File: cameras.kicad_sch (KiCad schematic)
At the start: 2 parts, among them J1 F32Q-1A7H1-11022, J2 F32Q-1A7H1-11022

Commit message: annotations, small fixes
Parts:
- renumbered J2 to J1, J1 to J2
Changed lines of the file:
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@@
 		(on_board yes)
 		(dnp no)
-		(property "Reference" "#PWR0134"
+		(property "Reference" "#PWR05"
 			(at 115.57 132.08 0)
 			(effects
@@
 			(project "CUTIE-CITRUS"
 				(path "/40af415e-5e3a-41a5-ab07-08c2181863e4/15df30c6-bd70-4c9b-9319-89653597e067"
-					(reference "#PWR0134")
+					(reference "#PWR05")
 					(unit 1)
 				)
@@
 		(on_board yes)
 		(dnp no)
-		(property "Reference" "#PWR0103"
+		(property "Reference" "#PWR06"
 			(at 200.66 132.08 0)
 			(effects
@@
 			(project "CUTIE-CITRUS"
 				(path "/40af415e-5e3a-41a5-ab07-08c2181863e4/15df30c6-bd70-4c9b-9319-89653597e067"
-					(reference "#PWR0103")
+					(reference "#PWR06")
 					(unit 1)
 				)
@@
 		(on_board yes)
 		(dnp no)
-		(property "Reference" "J2"
+		(property "Reference" "J1"
 			(at 128.27 63.5 0)
 			(effects
@@
 			(project "CUTIE-CITRUS"
 				(path "/40af415e-5e3a-41a5-ab07-08c2181863e4/15df30c6-bd70-4c9b-9319-89653597e067"
-					(reference "J2")
+					(reference "J1")
 					(unit 1)
 				)
@@
 		(on_board yes)
 		(dnp no)
-		(property "Reference" "J1"
+		(property "Reference" "J2"
 			(at 213.36 63.5 0)
 			(effects
@@
 			(project "CUTIE-CITRUS"
 				(path "/40af415e-5e3a-41a5-ab07-08c2181863e4/15df30c6-bd70-4c9b-9319-89653597e067"
-					(reference "J1")
+					(reference "J2")
 					(unit 1)
 				)

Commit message: extra abstraction layer for cm5 conns.
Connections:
- net SCL0 renamed I2C0.SCL
- net SCL1 renamed I2C1.SCL
- net SDA0 renamed I2C0.SDA
- net SDA1 renamed I2C1.SDA
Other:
- company: (none) -> Andre S Winkel | Highlander Space Program | University of California, Riverside
- title: (none) -> CUTIE-CITRUS PCB
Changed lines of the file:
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@@
 	(generator_version "9.0")
 	(paper "A4")
+	(title_block
+		(title "CUTIE-CITRUS PCB")
+		(date "2025-11-24")
+		(rev "A")
+		(company "Andre S Winkel | Highlander Space Program | University of California, Riverside")
+	)
 	(bus_alias "DPHY"
 		(members "D0_N" "D0_P" "D1_N" "D1_P" "C_N" "C_P" "D2_N" "D2_P" "D3_N" "D3_P")
@@
 	)
 	(bus_entry
+		(at 165.1 119.38)
+		(size 2.54 2.54)
+		(stroke
+			(width 0)
+			(type default)
+		)
+	)
+	(bus_entry
 		(at 165.1 88.9)
 		(size 2.54 2.54)
@@
 	)
 	(bus_entry
+		(at 165.1 116.84)
+		(size 2.54 2.54)
+		(stroke
+			(width 0)
+			(type default)
+		)
+	)
+	(bus_entry
 		(at 165.1 78.74)
 		(size 2.54 2.54)
@@
 	)
 	(bus_entry
+		(at 80.01 119.38)
+		(size 2.54 2.54)
+		(stroke
+			(width 0)
+			(type default)
+		)
+	)
+	(bus_entry
 		(at 165.1 93.98)
 		(size 2.54 2.54)
@@
 	)
 	(bus_entry
+		(at 80.01 116.84)
+		(size 2.54 2.54)
+		(stroke
+			(width 0)
+			(type default)
+		)
+	)
+	(bus_entry
 		(at 80.01 88.9)
 		(size 2.54 2.54)
@@
 		)
 	)
+	(bus
+		(pts
+			(xy 165.1 119.38) (xy 165.1 116.84)
+		)
+		(stroke
+			(width 0)
+			(type default)
+		)
+	)
 	(wire
 		(pts
@@
 		)
 	)
+	(bus
+		(pts
+			(xy 80.01 119.38) (xy 80.01 116.84)
+		)
+		(stroke
+			(width 0)
+			(type default)
+		)
+	)
+	(wire
+		(pts
+			(xy 82.55 119.38) (xy 118.11 119.38)
+		)
+		(stroke
+			(width 0)
+			(type default)
+		)
+	)
 	(wire
 		(pts
@@
 		)
 	)
-	(wire
-		(pts
-			(xy 161.29 121.92) (xy 203.2 121.92)
-		)
-		(stroke
-			(width 0)
-			(type solid)
-		)
-	)
 	(bus
 		(pts
@@
 	(wire
 		(pts
-			(xy 76.2 111.76) (xy 118.11 111.76)
+			(xy 99.06 111.76) (xy 118.11 111.76)
 		)
 		(stroke
@@
 	(wire
 		(pts
+			(xy 167.64 121.92) (xy 203.2 121.92)
+		)
+		(stroke
+			(width 0)
+			(type default)
+		)
+	)
+	(wire
+		(pts
 			(xy 200.66 78.74) (xy 203.2 78.74)
 		)
@@
 		)
 	)
-	(wire
-		(pts
-			(xy 76.2 114.3) (xy 118.11 114.3)
+	(bus
+		(pts
+			(xy 165.1 116.84) (xy 165.1 110.49)
+		)
+		(stroke
+			(width 0)
+			(type default)
+		)
+	)
+	(wire
+		(pts
+			(xy 99.06 114.3) (xy 118.11 114.3)
 		)
 		(stroke
@@
 	(bus
 		(pts
+			(xy 161.29 110.49) (xy 165.1 110.49)
+		)
+		(stroke
+			(width 0)
+			(type default)
+		)
+	)
+	(bus
+		(pts
 			(xy 80.01 78.74) (xy 80.01 81.28)
 		)
@@
 	(bus
 		(pts
+			(xy 80.01 116.84) (xy 80.01 110.49)
+		)
+		(stroke
+			(width 0)
+			(type default)
+		)
+	)
+	(wire
+		(pts
+			(xy 82.55 121.92) (xy 118.11 121.92)
+		)
+		(stroke
+			(width 0)
+			(type default)
+		)
+	)
+	(bus
+		(pts
 			(xy 80.01 88.9) (xy 80.01 93.98)
 		)
@@
 	(wire
 		(pts
-			(xy 76.2 121.92) (xy 118.11 121.92)
-		)
-		(stroke
-			(width 0)
-			(type solid)
-		)
-	)
-	(wire
-		(pts
 			(xy 167.64 104.14) (xy 203.2 104.14)
 		)
@@
 	(wire
 		(pts
-			(xy 76.2 119.38) (xy 118.11 119.38)
-		)
-		(stroke
-			(width 0)
-			(type solid)
-		)
-	)
-	(wire
-		(pts
 			(xy 167.64 73.66) (xy 203.2 73.66)
 		)
@@
 		)
 	)
+	(wire
+		(pts
+			(xy 167.64 119.38) (xy 203.2 119.38)
+		)
+		(stroke
+			(width 0)
+			(type default)
+		)
+	)
 	(bus
 		(pts
@@
 	(wire
 		(pts
-			(xy 161.29 119.38) (xy 203.2 119.38)
-		)
-		(stroke
-			(width 0)
-			(type solid)
-		)
-	)
-	(wire
-		(pts
 			(xy 82.55 73.66) (xy 118.11 73.66)
 		)
@@
 			(width 0)
 			(type solid)
+		)
+	)
+	(bus
+		(pts
+			(xy 76.2 110.49) (xy 80.01 110.49)
+		)
+		(stroke
+			(width 0)
+			(type default)
 		)
 	)
@@
 		)
 	)
-	(label "SDA1"
+	(label "I2C1.SDA"
 		(at 195.58 121.92 180)
 		(effects
@@
 		)
 	)
-	(label "SCL0"
+	(label "I2C0.SCL"
 		(at 110.49 119.38 180)
 		(effects
@@
 		)
 	)
-	(label "SCL1"
+	(label "I2C1.SCL"
 		(at 195.58 119.38 180)
 		(effects
@@
 		)
 	)
-	(label "SDA0"
+	(label "I2C0.SDA"
 		(at 110.49 121.92 180)
 		(effects
@@
 	(hierarchical_label "CAM_GPIO0"
 		(shape input)
-		(at 76.2 111.76 180)
+		(at 99.06 111.76 180)
 		(effects
 			(font
@@
 		)
 	)
-	(hierarchical_label "SCL0"
-		(shape input)
-		(at 76.2 119.38 180)
-		(effects
-			(font
-				(size 1.27 1.27)
-			)
-			(justify right)
-		)
-	)
-	(hierarchical_label "SDA1"
-		(shape input)
-		(at 161.29 121.92 180)
-		(effects
-			(font
-				(size 1.27 1.27)
-			)
-			(justify right)
-		)
-	)
 	(hierarchical_label "DPHY1{DPHY}"
 		(shape bidirectional)
@@
 		)
 	)
-	(hierarchical_label "SCL1"
-		(shape input)
-		(at 161.29 119.38 180)
+	(hierarchical_label "I2C0{I2C}"
+		(shape bidirectional)
+		(at 76.2 110.49 180)
 		(effects
 			(font
@@
 		)
 	)
-	(hierarchical_label "SDA0"
-		(shape input)
-		(at 76.2 121.92 180)
+	(hierarchical_label "I2C1{I2C}"
+		(shape bidirectional)
+		(at 161.29 110.49 180)
 		(effects
 			(font
@@
 	(hierarchical_label "CAM_GPIO1"
 		(shape input)
-		(at 76.2 114.3 180)
-		(effects
-			(font
+		(at 99.06 114.3 180)
+		(effects
+			(font

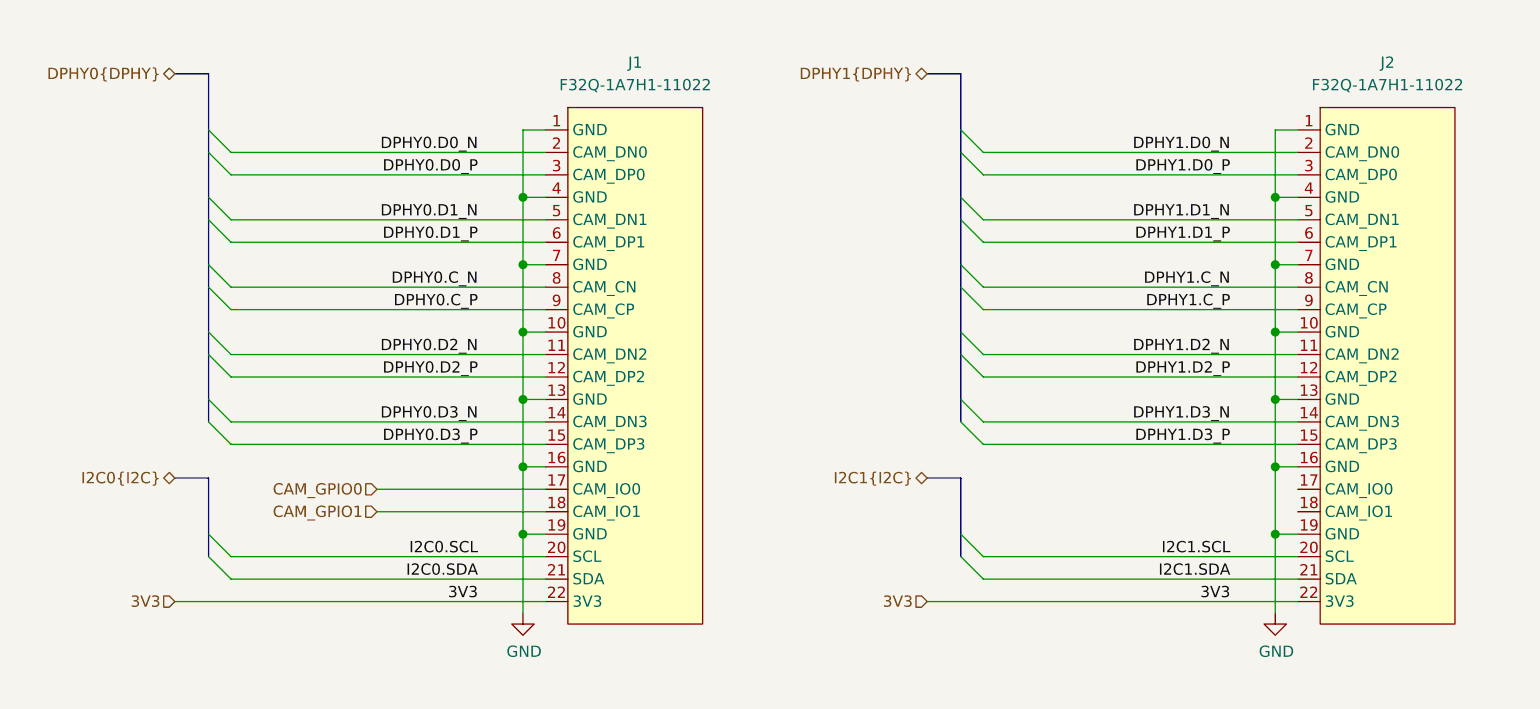
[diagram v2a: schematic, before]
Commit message: prepared usb3, abstracted cameras, backplane connector
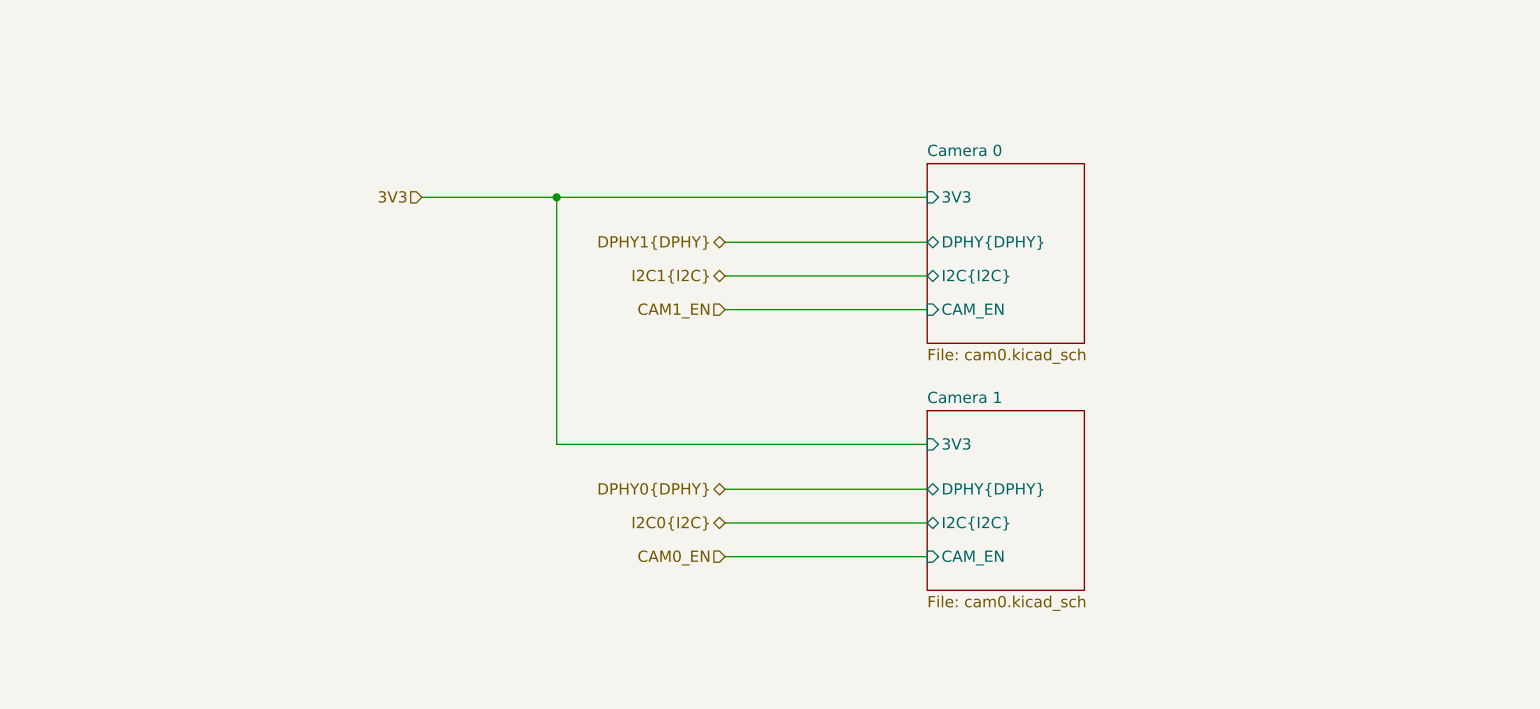
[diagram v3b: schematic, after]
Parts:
- removed J1, J2: F32Q-1A7H1-11022, library:Hirose_FH12-22S-0.5SH_1x22-1MP_P0.50mm_Horizontal, symbol library:F32Q-1A7H1-11022
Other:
- added sheet Camera 0 (cam0.kicad_sch)
- added sheet Camera 1 (cam0.kicad_sch)

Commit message: un-abstraction, footprints, layout edge cuts
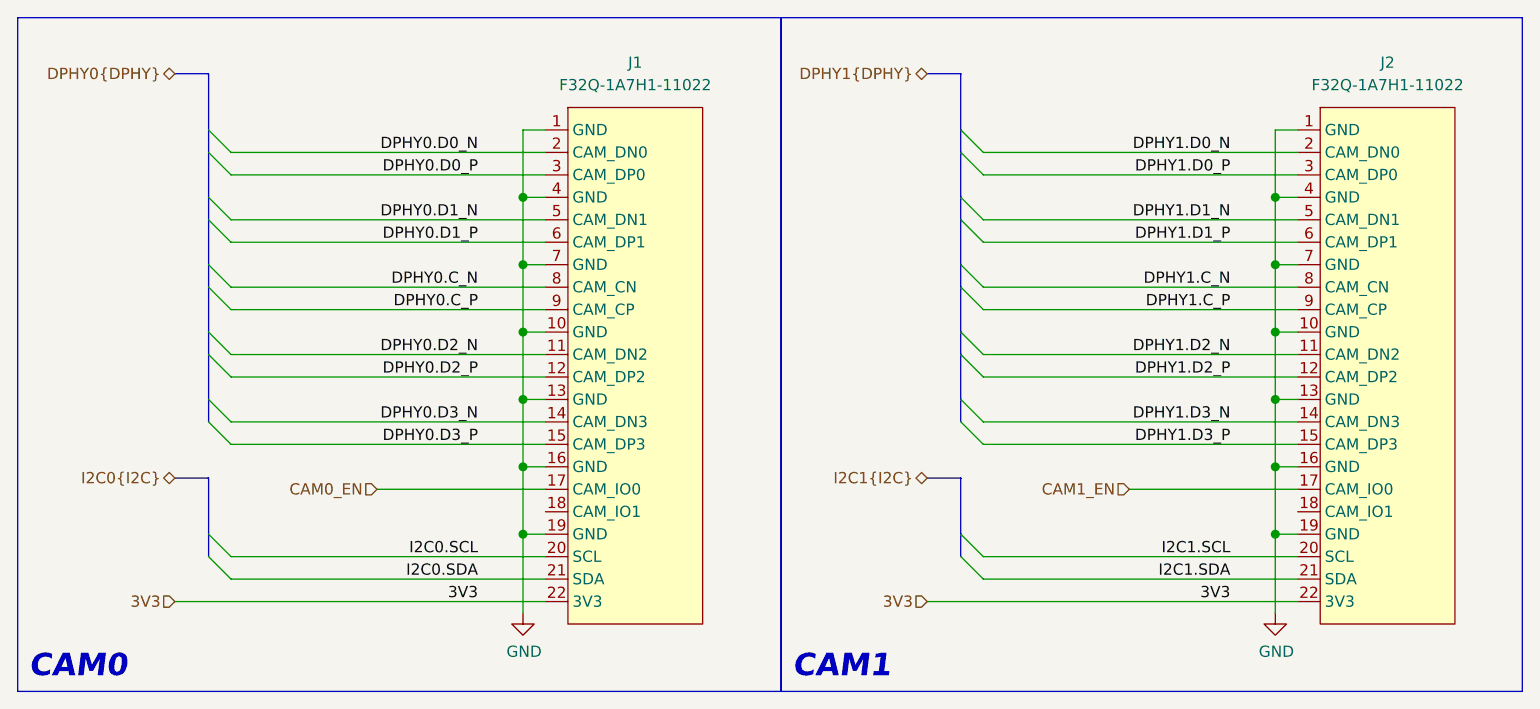
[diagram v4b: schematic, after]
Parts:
- added J1, J2: F32Q-1A7H1-11022, library:Hirose_FH12-22S-0.5SH_1x22-1MP_P0.50mm_Horizontal, symbol library:F32Q-1A7H1-11022
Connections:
- net 3V3: now also J1.22 (3V3), J2.22 (3V3)
- net CAM0_EN: now also J1.17 (CAM_IO0)
- net CAM1_EN: now also J2.17 (CAM_IO0)
- new net DPHY0.C_N: J1.8 (CAM_CN)
- new net DPHY0.C_P: J1.9 (CAM_CP)
- new net DPHY0.D0_N: J1.2 (CAM_DN0)
- new net DPHY0.D0_P: J1.3 (CAM_DP0)
- new net DPHY0.D1_N: J1.5 (CAM_DN1)
- new net DPHY0.D1_P: J1.6 (CAM_DP1)
- new net DPHY0.D2_N: J1.11 (CAM_DN2)
- new net DPHY0.D2_P: J1.12 (CAM_DP2)
- new net DPHY0.D3_N: J1.14 (CAM_DN3)
- new net DPHY0.D3_P: J1.15 (CAM_DP3)
- new net DPHY1.C_N: J2.8 (CAM_CN)
- new net DPHY1.C_P: J2.9 (CAM_CP)
- new net DPHY1.D0_N: J2.2 (CAM_DN0)
- new net DPHY1.D0_P: J2.3 (CAM_DP0)
- new net DPHY1.D1_N: J2.5 (CAM_DN1)
- new net DPHY1.D1_P: J2.6 (CAM_DP1)
- new net DPHY1.D2_N: J2.11 (CAM_DN2)
- new net DPHY1.D2_P: J2.12 (CAM_DP2)
- new net DPHY1.D3_N: J2.14 (CAM_DN3)
- new net DPHY1.D3_P: J2.15 (CAM_DP3)
- new net GND: J1.1 (GND), J1.10 (GND), J1.13 (GND), J1.16 (GND), J1.19 (GND), J1.4 (GND), J1.7 (GND), J2.1 (GND), J2.10 (GND), J2.13 (GND), J2.16 (GND), J2.19 (GND), J2.4 (GND), J2.7 (GND)
- new net I2C0.SCL: J1.20 (SCL)
- new net I2C0.SDA: J1.21 (SDA)
- new net I2C1.SCL: J2.20 (SCL)
- new net I2C1.SDA: J2.21 (SDA)
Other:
- removed sheet Camera 0
- removed sheet Camera 1
- note added: "CAM0"
- note added: "CAM1"

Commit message: redid gpio layout, removed one temp sensor, bom
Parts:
- J1, J2: Manufacturer (none) -> Amphenol ICC (FCI); Manufacturer Product Number (none) -> F32Q-1A7H1-11022
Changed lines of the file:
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@@
+			)
+		)
+		(property "Manufacturer" "Amphenol ICC (FCI)"
+			(at 128.27 97.79 0)
+			(effects
+				(font
+					(size 1.27 1.27)
+				)
+				(hide yes)
+			)
+		)
+		(property "Manufacturer Product Number" "F32Q-1A7H1-11022"
+			(at 128.27 97.79 0)
+			(effects
+				(font
+					(size 1.27 1.27)
+				)
+				(hide yes)
 			)
 		)
@@
 			(effects
 				(font
+					(size 1.27 1.27)
+				)
+				(hide yes)
+			)
+		)
+		(property "Manufacturer" "Amphenol ICC (FCI)"
+			(at 213.36 97.79 0)
+			(effects
+				(font
+					(size 1.27 1.27)
+				)
+				(hide yes)
+			)
+		)
+		(property "Manufacturer Product Number" "F32Q-1A7H1-11022"
+			(at 213.36 97.79 0)
+			(effects
+				(font
